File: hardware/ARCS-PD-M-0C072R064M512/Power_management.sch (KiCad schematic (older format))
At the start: 27 parts

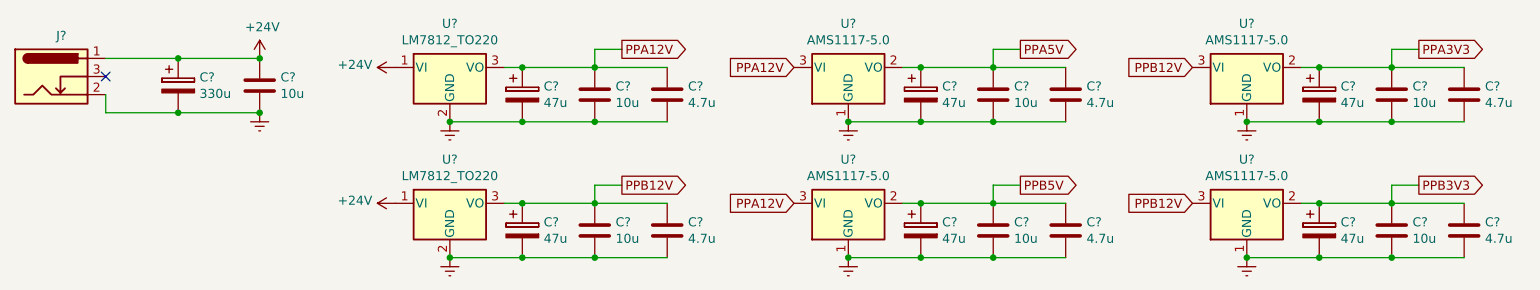
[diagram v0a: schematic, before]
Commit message: Create cards for input and output interface.
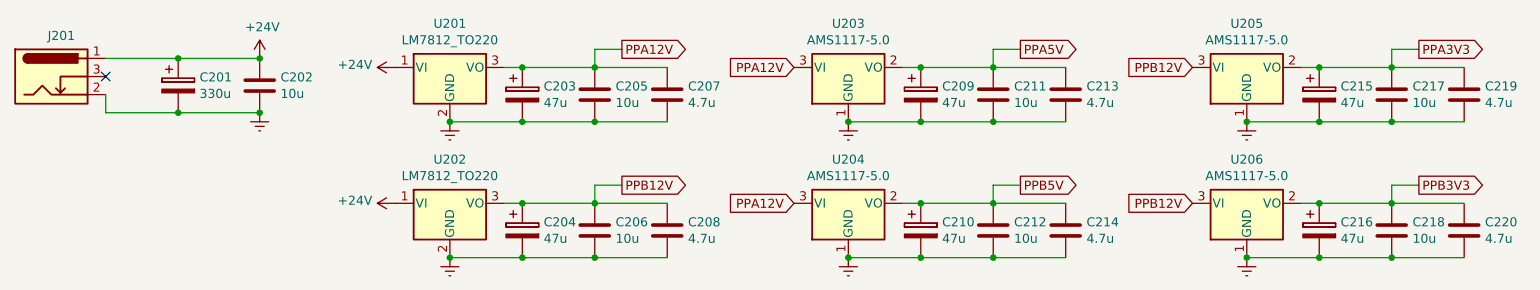
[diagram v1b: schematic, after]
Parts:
- gave numbers to parts that had none: 27
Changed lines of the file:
@@
 $EndDescr
 $Comp
-L Regulator_Linear:LM7812_TO220 U?
+L Regulator_Linear:LM7812_TO220 U201
 U 1 1 5C602CDD
 P 3600 1200
-F 0 "U?" H 3600 1442 50  0000 C CNN
+F 0 "U201" H 3600 1442 50  0000 C CNN
 F 1 "LM7812_TO220" H 3600 1351 50  0000 C CNN
 F 2 "Package_TO_SOT_THT:TO-220-3_Vertical" H 3600 1425 50  0001 C CIN
@@
 $EndComp
 $Comp
-L Connector:Barrel_Jack_Switch J?
+L Connector:Barrel_Jack_Switch J201
 U 1 1 5C602E7F
 P 1400 1250
-F 0 "J?" H 1455 1475 50  0000 C CNN
+F 0 "J201" H 1455 1475 50  0000 C CNN
 F 1 "Barrel_Jack_Switch" H 1455 1476 50  0001 C CNN
 F 2 "" H 1450 1210 50  0001 C CNN
@@
 $EndComp
 $Comp
-L Device:CP C?
+L Device:CP C201
 U 1 1 5C602FE8
 P 2100 1300
-F 0 "C?" H 2218 1346 50  0000 L CNN
+F 0 "C201" H 2218 1346 50  0000 L CNN
 F 1 "330u" H 2218 1255 50  0000 L CNN
 F 2 "" H 2138 1150 50  0001 C CNN
@@
 $EndComp
 $Comp
-L Device:C C?
+L Device:C C202
 U 1 1 5C603061
 P 2550 1300
-F 0 "C?" H 2665 1346 50  0000 L CNN
+F 0 "C202" H 2665 1346 50  0000 L CNN
 F 1 "10u" H 2665 1255 50  0000 L CNN
 F 2 "" H 2588 1150 50  0001 C CNN
@@
 NoConn ~ 1700 1250
 $Comp
-L power:+24V #PWR?
+L power:+24V #PWR0201
 U 1 1 5C6031D4
 P 2550 1150
-F 0 "#PWR?" H 2550 1000 50  0001 C CNN
+F 0 "#PWR0201" H 2550 1000 50  0001 C CNN
 F 1 "+24V" H 2565 1323 50  0000 C CNN
 F 2 "" H 2550 1150 50  0001 C CNN
@@
 $EndComp
 $Comp
-L power:Earth #PWR?
+L power:Earth #PWR0202
 U 1 1 5C603256
 P 2550 1450
-F 0 "#PWR?" H 2550 1200 50  0001 C CNN
+F 0 "#PWR0202" H 2550 1200 50  0001 C CNN
 F 1 "Earth" H 2550 1300 50  0001 C CNN
 F 2 "" H 2550 1450 50  0001 C CNN
@@
 	2100 1150 2550 1150
 $Comp
-L power:Earth #PWR?
+L power:Earth #PWR0205
 U 1 1 5C603418
 P 3600 1500
-F 0 "#PWR?" H 3600 1250 50  0001 C CNN
+F 0 "#PWR0205" H 3600 1250 50  0001 C CNN
 F 1 "Earth" H 3600 1350 50  0001 C CNN
 F 2 "" H 3600 1500 50  0001 C CNN
@@
 $EndComp
 $Comp
-L Device:CP C?
+L Device:CP C203
 U 1 1 5C603437
 P 4000 1350
-F 0 "C?" H 4118 1396 50  0000 L CNN
+F 0 "C203" H 4118 1396 50  0000 L CNN
 F 1 "47u" H 4118 1305 50  0000 L CNN
 F 2 "" H 4038 1200 50  0001 C CNN
@@
 $EndComp
 $Comp
-L Device:C C?
+L Device:C C205
 U 1 1 5C6034B8
 P 4400 1350
-F 0 "C?" H 4515 1396 50  0000 L CNN
+F 0 "C205" H 4515 1396 50  0000 L CNN
 F 1 "10u" H 4515 1305 50  0000 L CNN
 F 2 "" H 4438 1200 50  0001 C CNN
@@
 $EndComp
 $Comp
-L Device:C C?
+L Device:C C207
 U 1 1 5C6034FC
 P 4800 1350
-F 0 "C?" H 4915 1396 50  0000 L CNN
+F 0 "C207" H 4915 1396 50  0000 L CNN
 F 1 "4.7u" H 4915 1305 50  0000 L CNN
 F 2 "" H 4838 1200 50  0001 C CNN
@@
 	4400 1500 4000 1500
 $Comp
-L power:+24V #PWR?
+L power:+24V #PWR0203
 U 1 1 5C6035E0
 P 3300 1200
-F 0 "#PWR?" H 3300 1050 50  0001 C CNN
+F 0 "#PWR0203" H 3300 1050 50  0001 C CNN
 F 1 "+24V" V 3315 1328 50  0000 L CNN
 F 2 "" H 3300 1200 50  0001 C CNN
@@
 	4400 1100 4400 1200
 $Comp
-L Regulator_Linear:AMS1117-5.0 U?
+L Regulator_Linear:AMS1117-5.0 U203
 U 1 1 5C60389F
 P 5800 1200
-F 0 "U?" H 5800 1442 50  0000 C CNN
+F 0 "U203" H 5800 1442 50  0000 C CNN
 F 1 "AMS1117-5.0" H 5800 1351 50  0000 C CNN
 F 2 "Package_TO_SOT_SMD:SOT-223-3_TabPin2" H 5800 1400 50  0001 C CNN
@@
 $EndComp
 $Comp
-L Device:CP C?
+L Device:CP C209
 U 1 1 5C603A15
 P 6200 1350
-F 0 "C?" H 6318 1396 50  0000 L CNN
+F 0 "C209" H 6318 1396 50  0000 L CNN
 F 1 "47u" H 6318 1305 50  0000 L CNN
 F 2 "" H 6238 1200 50  0001 C CNN
@@
 $EndComp
 $Comp
-L Device:C C?
+L Device:C C211
 U 1 1 5C603A57
 P 6600 1350
-F 0 "C?" H 6715 1396 50  0000 L CNN
+F 0 "C211" H 6715 1396 50  0000 L CNN
 F 1 "10u" H 6715 1305 50  0000 L CNN
 F 2 "" H 6638 1200 50  0001 C CNN
@@
 $EndComp
 $Comp
-L Device:C C?
+L Device:C C213
 U 1 1 5C603A99
 P 7000 1350
-F 0 "C?" H 7115 1396 50  0000 L CNN
+F 0 "C213" H 7115 1396 50  0000 L CNN
 F 1 "4.7u" H 7115 1305 50  0000 L CNN
 F 2 "" H 7038 1200 50  0001 C CNN
@@
 	6600 1500 6200 1500
 $Comp
-L power:Earth #PWR?
+L power:Earth #PWR0207
 U 1 1 5C603D73
 P 5800 1500
-F 0 "#PWR?" H 5800 1250 50  0001 C CNN
+F 0 "#PWR0207" H 5800 1250 50  0001 C CNN
 F 1 "Earth" H 5800 1350 50  0001 C CNN
 F 2 "" H 5800 1500 50  0001 C CNN
@@
 PPA12V
 $Comp
-L Regulator_Linear:AMS1117-5.0 U?
+L Regulator_Linear:AMS1117-5.0 U205
 U 1 1 5C6043FD
 P 8000 1200
-F 0 "U?" H 8000 1442 50  0000 C CNN
+F 0 "U205" H 8000 1442 50  0000 C CNN
 F 1 "AMS1117-5.0" H 8000 1351 50  0000 C CNN
 F 2 "Package_TO_SOT_SMD:SOT-223-3_TabPin2" H 8000 1400 50  0001 C CNN
@@
 $EndComp
 $Comp
-L Device:CP C?
+L Device:CP C215
 U 1 1 5C604404
 P 8400 1350
-F 0 "C?" H 8518 1396 50  0000 L CNN
+F 0 "C215" H 8518 1396 50  0000 L CNN
 F 1 "47u" H 8518 1305 50  0000 L CNN
 F 2 "" H 8438 1200 50  0001 C CNN
@@
 $EndComp
 $Comp
-L Device:C C?
+L Device:C C217
 U 1 1 5C60440B
 P 8800 1350
-F 0 "C?" H 8915 1396 50  0000 L CNN
+F 0 "C217" H 8915 1396 50  0000 L CNN
 F 1 "10u" H 8915 1305 50  0000 L CNN
 F 2 "" H 8838 1200 50  0001 C CNN
@@
 $EndComp
 $Comp
-L Device:C C?
+L Device:C C219
 U 1 1 5C604412
 P 9200 1350
-F 0 "C?" H 9315 1396 50  0000 L CNN
+F 0 "C219" H 9315 1396 50  0000 L CNN
 F 1 "4.7u" H 9315 1305 50  0000 L CNN
 F 2 "" H 9238 1200 50  0001 C CNN
@@
 	8800 1500 8400 1500
 $Comp
-L power:Earth #PWR?
+L power:Earth #PWR0209
 U 1 1 5C604423
 P 8000 1500
-F 0 "#PWR?" H 8000 1250 50  0001 C CNN
+F 0 "#PWR0209" H 8000 1250 50  0001 C CNN
 F 1 "Earth" H 8000 1350 50  0001 C CNN
 F 2 "" H 8000 1500 50  0001 C CNN
@@
 PPB12V
 $Comp
-L Regulator_Linear:AMS1117-5.0 U?
+L Regulator_Linear:AMS1117-5.0 U204
 U 1 1 5C8A908D
 P 5800 1950
-F 0 "U?" H 5800 2192 50  0000 C CNN
+F 0 "U204" H 5800 2192 50  0000 C CNN
 F 1 "AMS1117-5.0" H 5800 2101 50  0000 C CNN
 F 2 "Package_TO_SOT_SMD:SOT-223-3_TabPin2" H 5800 2150 50  0001 C CNN
@@
 $EndComp
 $Comp
-L Device:CP C?
+L Device:CP C210
 U 1 1 5C8A9094
 P 6200 2100
-F 0 "C?" H 6318 2146 50  0000 L CNN
+F 0 "C210" H 6318 2146 50  0000 L CNN
 F 1 "47u" H 6318 2055 50  0000 L CNN
 F 2 "" H 6238 1950 50  0001 C CNN
@@
 $EndComp
 $Comp
-L Device:C C?
+L Device:C C212
 U 1 1 5C8A909B
 P 6600 2100
-F 0 "C?" H 6715 2146 50  0000 L CNN
+F 0 "C212" H 6715 2146 50  0000 L CNN
 F 1 "10u" H 6715 2055 50  0000 L CNN
 F 2 "" H 6638 1950 50  0001 C CNN
@@
 $EndComp
 $Comp
-L Device:C C?
+L Device:C C214
 U 1 1 5C8A90A2
 P 7000 2100
-F 0 "C?" H 7115 2146 50  0000 L CNN
+F 0 "C214" H 7115 2146 50  0000 L CNN
 F 1 "4.7u" H 7115 2055 50  0000 L CNN
 F 2 "" H 7038 1950 50  0001 C CNN
@@
 	6600 2250 6200 2250
 $Comp
-L power:Earth #PWR?
+L power:Earth #PWR0208
 U 1 1 5C8A90B3
 P 5800 2250
-F 0 "#PWR?" H 5800 2000 50  0001 C CNN
+F 0 "#PWR0208" H 5800 2000 50  0001 C CNN
 F 1 "Earth" H 5800 2100 50  0001 C CNN
 F 2 "" H 5800 2250 50  0001 C CNN
@@
 PPA12V
 $Comp
-L Regulator_Linear:AMS1117-5.0 U?
+L Regulator_Linear:AMS1117-5.0 U206
 U 1 1 5C8AE567
 P 8000 1950
-F 0 "U?" H 8000 2192 50  0000 C CNN
+F 0 "U206" H 8000 2192 50  0000 C CNN
 F 1 "AMS1117-5.0" H 8000 2101 50  0000 C CNN
 F 2 "Package_TO_SOT_SMD:SOT-223-3_TabPin2" H 8000 2150 50  0001 C CNN
@@
 $EndComp
 $Comp
-L Device:CP C?
+L Device:CP C216
 U 1 1 5C8AE56E
 P 8400 2100
-F 0 "C?" H 8518 2146 50  0000 L CNN
+F 0 "C216" H 8518 2146 50  0000 L CNN
 F 1 "47u" H 8518 2055 50  0000 L CNN
 F 2 "" H 8438 1950 50  0001 C CNN
@@
 $EndComp
 $Comp
-L Device:C C?
+L Device:C C218
 U 1 1 5C8AE575
 P 8800 2100
-F 0 "C?" H 8915 2146 50  0000 L CNN
+F 0 "C218" H 8915 2146 50  0000 L CNN
 F 1 "10u" H 8915 2055 50  0000 L CNN
 F 2 "" H 8838 1950 50  0001 C CNN
@@
 $EndComp
 $Comp
-L Device:C C?
+L Device:C C220
 U 1 1 5C8AE57C
 P 9200 2100
-F 0 "C?" H 9315 2146 50  0000 L CNN
+F 0 "C220" H 9315 2146 50  0000 L CNN
 F 1 "4.7u" H 9315 2055 50  0000 L CNN
 F 2 "" H 9238 1950 50  0001 C CNN
@@
 	8800 2250 8400 2250
 $Comp
-L power:Earth #PWR?
+L power:Earth #PWR0210
 U 1 1 5C8AE58D
 P 8000 2250
-F 0 "#PWR?" H 8000 2000 50  0001 C CNN
+F 0 "#PWR0210" H 8000 2000 50  0001 C CNN
 F 1 "Earth" H 8000 2100 50  0001 C CNN
 F 2 "" H 8000 2250 50  0001 C CNN
@@
 PPB12V
 $Comp
-L Regulator_Linear:LM7812_TO220 U?
+L Regulator_Linear:LM7812_TO220 U202
 U 1 1 5C8AF11F
 P 3600 1950
-F 0 "U?" H 3600 2192 50  0000 C CNN
+F 0 "U202" H 3600 2192 50  0000 C CNN
 F 1 "LM7812_TO220" H 3600 2101 50  0000 C CNN
 F 2 "Package_TO_SOT_THT:TO-220-3_Vertical" H 3600 2175 50  0001 C CIN
@@
 $EndComp
 $Comp
-L power:Earth #PWR?
+L power:Earth #PWR0206
 U 1 1 5C8AF126
 P 3600 2250
-F 0 "#PWR?" H 3600 2000 50  0001 C CNN
+F 0 "#PWR0206" H 3600 2000 50  0001 C CNN
 F 1 "Earth" H 3600 2100 50  0001 C CNN
 F 2 "" H 3600 2250 50  0001 C CNN
@@
 $EndComp
 $Comp
-L Device:CP C?
+L Device:CP C204
 U 1 1 5C8AF12C
 P 4000 2100
-F 0 "C?" H 4118 2146 50  0000 L CNN
+F 0 "C204" H 4118 2146 50  0000 L CNN
 F 1 "47u" H 4118 2055 50  0000 L CNN
 F 2 "" H 4038 1950 50  0001 C CNN
@@
 $EndComp
 $Comp
-L Device:C C?
+L Device:C C206
 U 1 1 5C8AF133
 P 4400 2100
-F 0 "C?" H 4515 2146 50  0000 L CNN
+F 0 "C206" H 4515 2146 50  0000 L CNN
 F 1 "10u" H 4515 2055 50  0000 L CNN
 F 2 "" H 4438 1950 50  0001 C CNN
@@
 $EndComp
 $Comp
-L Device:C C?
+L Device:C C208
 U 1 1 5C8AF13A
 P 4800 2100
-F 0 "C?" H 4915 2146 50  0000 L CNN
+F 0 "C208" H 4915 2146 50  0000 L CNN
 F 1 "4.7u" H 4915 2055 50  0000 L CNN
 F 2 "" H 4838 1950 50  0001 C CNN
@@
 	4400 2250 4000 2250
 $Comp
-L power:+24V #PWR?
+L power:+24V #PWR0204
 U 1 1 5C8AF14C
 P 3300 1950
-F 0 "#PWR?" H 3300 1800 50  0001 C CNN
+F 0 "#PWR0204" H 3300 1800 50  0001 C CNN
 F 1 "+24V" V 3315 2078 50  0000 L CNN
 F 2 "" H 3300 1950 50  0001 C CNN
